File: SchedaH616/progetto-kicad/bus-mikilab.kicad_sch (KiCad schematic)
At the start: 6 parts, among them J1 BUS_POWER_MIKILAB, J2 BUS_MIKILAB_MAIN

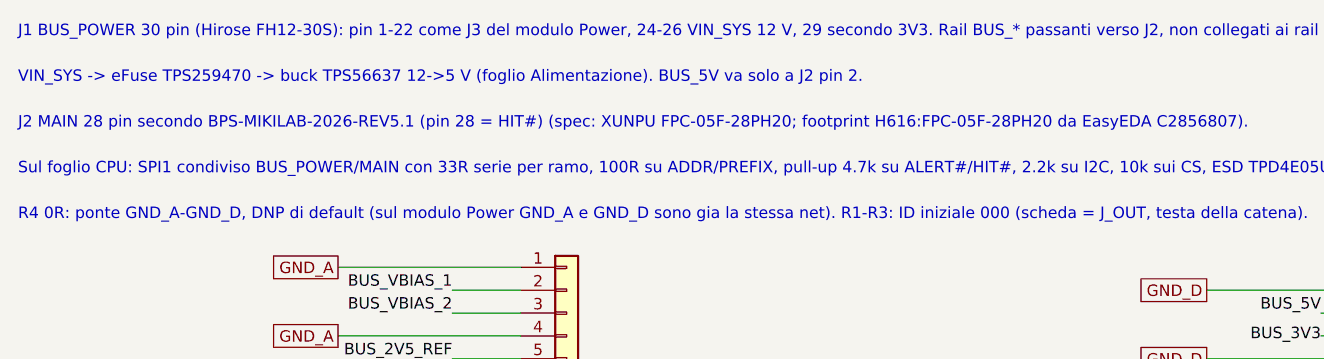
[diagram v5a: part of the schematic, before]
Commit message: SchedaH616: eFuse TPS259470 eliminato
- tolti U106 TPS259470 e i suoi componenti (partitore UVLO/OVLO, RILM, dVdT, 1 uF d'ingresso) e il footprint RPW dalla libreria
- VIN_SYS dal BUS_POWER direttamente all'ingresso del TPS56637 (restano C101/C102 10 uF e C125 100 nF)
- ingresso 12 V senza limite di corrente, OVP ne' blocco inverso; nessuna TVS sui 12 V
- P17 del TCA6416A ora libera; documenti aggiornati
- ERC 0, parita' 0, DRC 0 (solo collegamenti da fare)

Co-Authored-By: Claude Opus 5.5 (1M context) <noreply@anthropic.com>
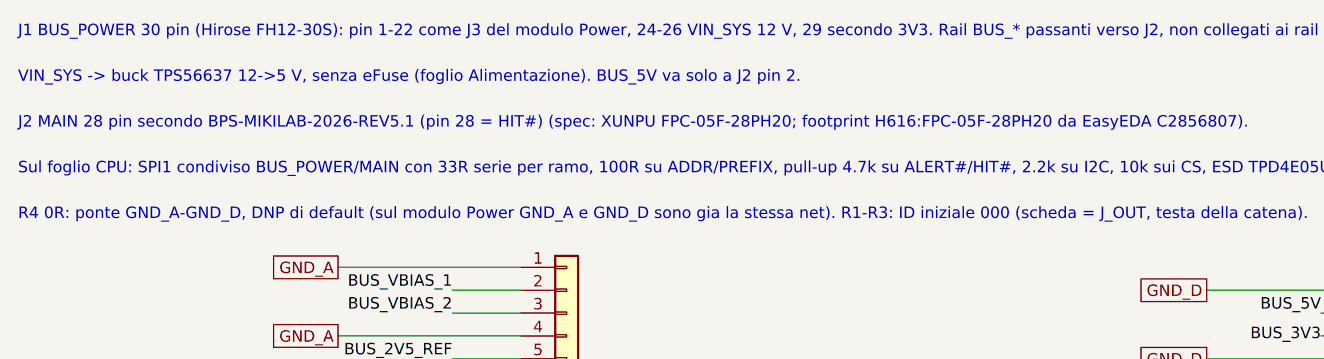
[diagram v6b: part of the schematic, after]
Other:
- note added: "VIN_SYS -> buck TPS56637 12->5 V, senza eFuse (foglio Alimentazione). BUS_5V va solo a J2 pin 2."
- note removed: "VIN_SYS -> eFuse TPS259470 -> buck TPS56637 12->5 V (foglio Alimentazione). BUS_5V va solo a J2 pin 2."

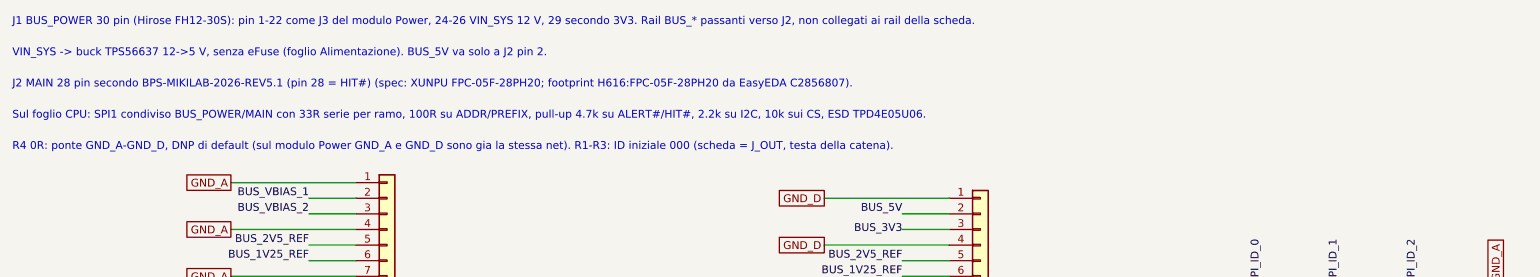
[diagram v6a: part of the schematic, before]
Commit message: SchedaH616: RK3568 + RK809-5 + TCS4525 + DDR4, placement 50x70
- SoC Allwinner H616 -> Rockchip RK3568 (FCBGA636L, LCSC C2938930): ball map dal pinout
  Rockchip V1.1, verificata sulla tabella 2-1 del datasheet V1.2 (636/636); footprint
  generato (gen_fp.py), confrontato con EasyEDA C2938930
- PMIC AXP313A -> RK809-5 (C2939628) come Rockchip AIoT REF V1.1 / ROCK 3A; TCS4525 per
  VDD_CPU su I2C0 (0x1C); BUCK4 su VDD_NPU (sull'RK809-5 parte spento: non puo' fare il 3.3 V)
- LPDDR4 -> DDR4 x16 K4AAG165WA-BCWE (C2920140) sul canale A, point-to-point, niente VTT,
  VPP da AP2112K-2.5, ZQ 240R, DDR_RZQ del SoC 120R (Hardware Design Guide)
- eMMC su EMMC 8 bit (VCCIO2 1.8 V), microSD su SDMMC0, AP6256 su SDMMC2 + UART8,
  RTL8211F su GMAC0 RGMII (22R TX al SoC e RX al PHY), console UART2_M0, USB-C su OTG0
- Recovery su SARADC_VIN0, reset sulla rete RESETn; TCA6416A tolto
- Bus MIKILAB: BUS_POWER su SPI3_M1, MAIN su SPI2_M1 (CS del DAC su cs-gpios)
- progetto rinominato SchedaRK3568, libreria di progetto Scheda; script portabili Linux/macOS
- ERC 0, parita' 0, DRC 0 (solo collegamenti da fare); placement 439/439

Co-Authored-By: Claude Opus 5.5 (1M context) <noreply@anthropic.com>
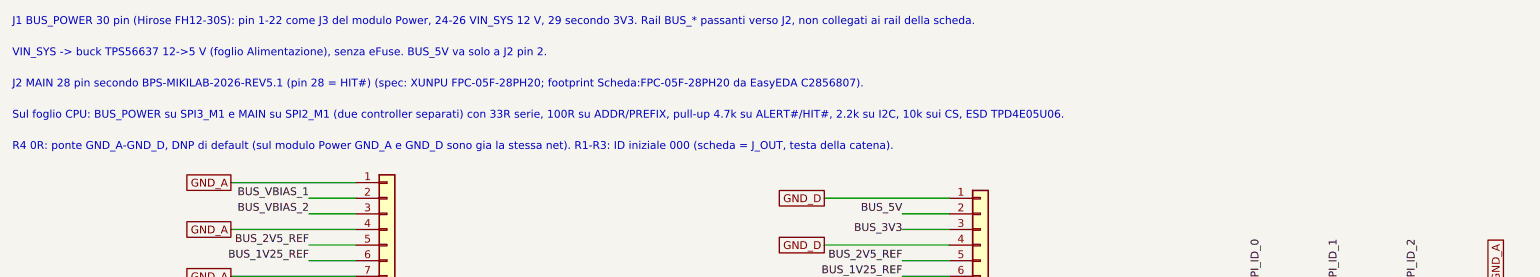
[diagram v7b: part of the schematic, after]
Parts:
- J2: footprint H616:FPC-05F-28PH20 -> Scheda:FPC-05F-28PH20
- R1, R2, R3, R4: footprint Resistor_SMD:R_0603_1608Metric -> Resistor_SMD:R_0402_1005Metric
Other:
- note added: "J2 MAIN 28 pin secondo BPS-MIKILAB-2026-REV5.1 (pin 28 = HIT#) (spec: XUNPU FPC-05F-28PH20; footprint Scheda:FPC-05F-28PH20 da EasyEDA C2856807)."
- note added: "Sul foglio CPU: BUS_POWER su SPI3_M1 e MAIN su SPI2_M1 (due controller separati) con 33R serie, 100R su ADDR/PREFIX, pull-up 4.7k su ALERT#/HIT#, 2.2k su I2C, 10k sui CS, ESD TPD4E05U06."
- note added: "VIN_SYS -> buck TPS56637 12->5 V (foglio Alimentazione), senza eFuse. BUS_5V va solo a J2 pin 2."
- note removed: "J2 MAIN 28 pin secondo BPS-MIKILAB-2026-REV5.1 (pin 28 = HIT#) (spec: XUNPU FPC-05F-28PH20; footprint H616:FPC-05F-28PH20 da EasyEDA C2856807)."
- note removed: "Sul foglio CPU: SPI1 condiviso BUS_POWER/MAIN con 33R serie per ramo, 100R su ADDR/PREFIX, pull-up 4.7k su ALERT#/HIT#, 2.2k su I2C, 10k sui CS, ESD TPD4E05U06."
- note removed: "VIN_SYS -> buck TPS56637 12->5 V, senza eFuse (foglio Alimentazione). BUS_5V va solo a J2 pin 2."

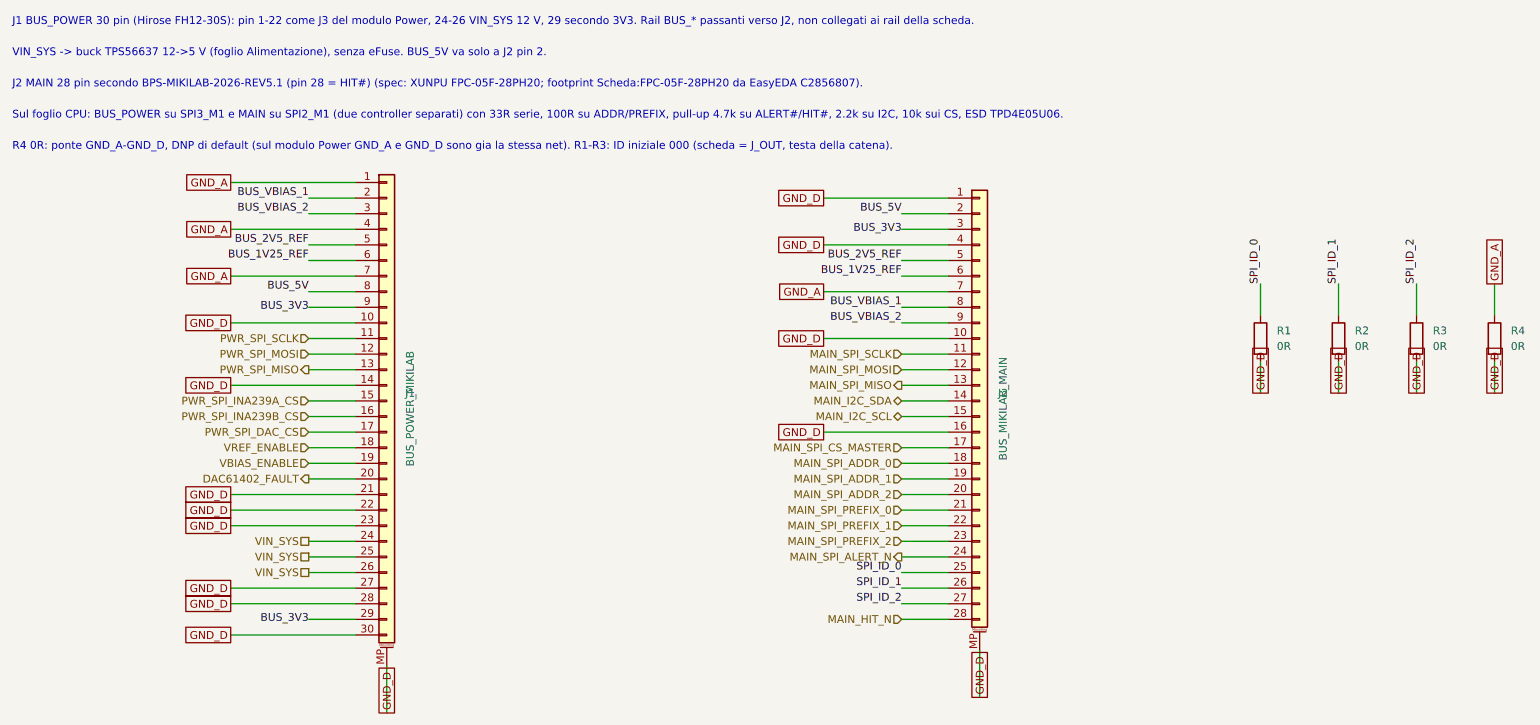
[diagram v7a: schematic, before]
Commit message: SchedaH616: componenti specifici dalla libreria MIKILAB
- simbolo e footprint MIKILAB per RK809-5, TCS4525, K4AAG165WA-BCWE, FEMDNN064G-C9A61,
  AP2112K-1.8TRG1, TPS56637RPAR, TPS2121RUXR, SY6280AAC, TPS563201DDCR, TPS2553DBVR,
  TYPE-C-31-M-12, FH12-30S-0.5SH, FPC-05F-28PH20, HR911130C, 25AA02E48T-I/OT, DM3AT-SF-PEJM5;
  simbolo MIKILAB per l'AP6256
- restano nella libreria di progetto: RK3568 (pad EasyEDA da 0.35 mm, niente fanout 5/5 mil),
  simbolo RTL8211F (quello MIKILAB ha pin di alimentazione nascosti), footprint AP6256 LGA-47,
  portapila BS-12; motivazioni in docs/scelte-progetto.md
- kilib.mik() carica simboli e footprint dalla libreria (variabile MIKILAB); matrice ERC:
  pin unspecified dei simboli EasyEDA OK
- netlist identica a 4ca35fc (439 componenti, 314 net); ERC 0, parita' 0, DRC 0 (solo
  collegamenti da fare); footprint corretti nella libreria MIKILAB 8b990c4

Co-Authored-By: Claude Opus 5.5 (1M context) <noreply@anthropic.com>
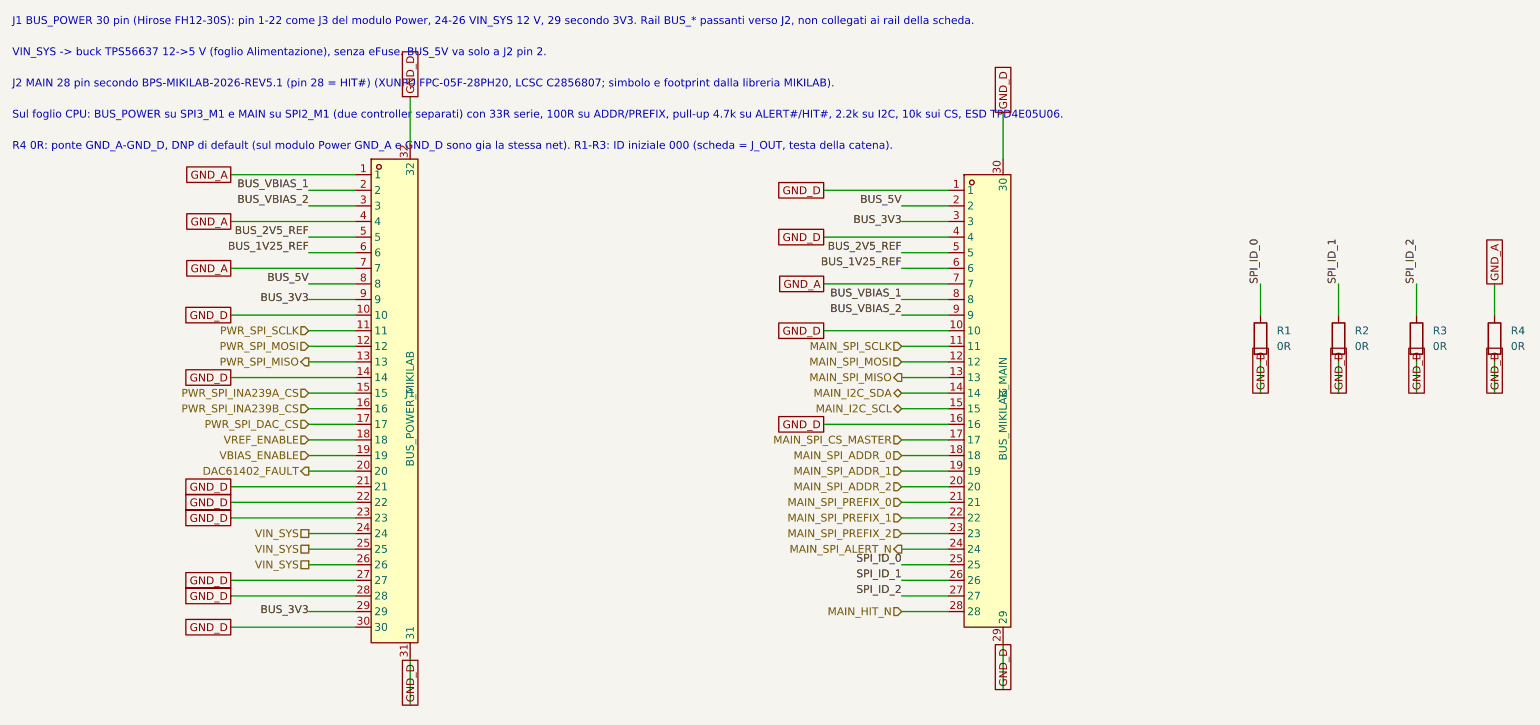
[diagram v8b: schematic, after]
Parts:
- removed J1: BUS_POWER_MIKILAB, Connector_FFC-FPC:Hirose_FH12-30S-0.5SH_1x30-1MP_P0.50mm_Horizontal, symbol Connector_Generic_MountingPin:Conn_01x30_MountingPin
- removed J2: BUS_MIKILAB_MAIN, Scheda:FPC-05F-28PH20, symbol Connector_Generic_MountingPin:Conn_01x28_MountingPin
- added J1: BUS_POWER_MIKILAB, MIKILAB_FH12_30S_0_5SH:FPC-SMD_FH12-30S-0.5SH-55, symbol MIKILAB_FH12_30S_0_5SH:FH12-30S-0.5SH
- added J2: BUS_MIKILAB_MAIN, MIKILAB_FPC_05F_28PH20:FPC-SMD_28P-P0.50_FPC-05F-28PH20, symbol MIKILAB_FPC_05F_28PH20:FPC-05F-28PH20
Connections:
- net BUS_1V25_REF: now also J1.6, J2.6
- net BUS_2V5_REF: now also J1.5, J2.5
- net BUS_3V3: now also J1.29, J1.9, J2.3
- net BUS_5V: now also J1.8, J2.2
- net BUS_VBIAS_1: now also J1.2, J2.8
- net BUS_VBIAS_2: now also J1.3, J2.9
- net DAC61402_FAULT: now also J1.20
- net GND_A: now also J1.1, J1.4, J1.7, J2.7
- net GND_D: now also J1.10, J1.14, J1.21, J1.22, J1.23, J1.27, J1.28, J1.30, J1.31, J1.32, J2.1, J2.10, J2.16, J2.29, J2.30, J2.4
- net MAIN_HIT_N: now also J2.28
- net MAIN_I2C_SCL: now also J2.15
- net MAIN_I2C_SDA: now also J2.14
- net MAIN_SPI_ADDR_0: now also J2.18
- net MAIN_SPI_ADDR_1: now also J2.19
- net MAIN_SPI_ADDR_2: now also J2.20
- net MAIN_SPI_ALERT_N: now also J2.24
- net MAIN_SPI_CS_MASTER: now also J2.17
- net MAIN_SPI_MISO: now also J2.13
- net MAIN_SPI_MOSI: now also J2.12
- net MAIN_SPI_PREFIX_0: now also J2.21
- net MAIN_SPI_PREFIX_1: now also J2.22
- net MAIN_SPI_PREFIX_2: now also J2.23
- net MAIN_SPI_SCLK: now also J2.11
- net PWR_SPI_DAC_CS: now also J1.17
- net PWR_SPI_INA239A_CS: now also J1.15
- net PWR_SPI_INA239B_CS: now also J1.16
- net PWR_SPI_MISO: now also J1.13
- net PWR_SPI_MOSI: now also J1.12
- net PWR_SPI_SCLK: now also J1.11
- net SPI_ID_0: now also J2.25
- net SPI_ID_1: now also J2.26
- net SPI_ID_2: now also J2.27
- net VBIAS_ENABLE: now also J1.19
- net VIN_SYS: now also J1.24, J1.25, J1.26
- net VREF_ENABLE: now also J1.18
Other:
- note added: "J2 MAIN 28 pin secondo BPS-MIKILAB-2026-REV5.1 (pin 28 = HIT#) (XUNPU FPC-05F-28PH20, LCSC C2856807; simbolo e footprint dalla libreria MIKILAB)."
- note removed: "J2 MAIN 28 pin secondo BPS-MIKILAB-2026-REV5.1 (pin 28 = HIT#) (spec: XUNPU FPC-05F-28PH20; footprint Scheda:FPC-05F-28PH20 da EasyEDA C2856807)."
